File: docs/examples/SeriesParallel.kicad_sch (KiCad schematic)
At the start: 3 parts

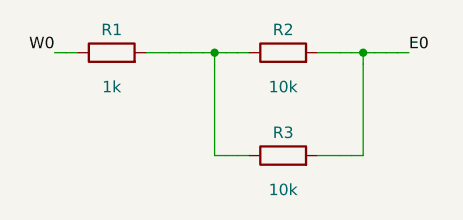
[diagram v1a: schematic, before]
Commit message: ERC-clean KiCad export: project + sym-lib-table, test points on open ports, automatic PWR_FLAGs from geometry nets; ERC (errors+warnings) asserted in tests
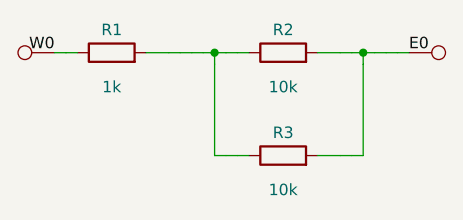
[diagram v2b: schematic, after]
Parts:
- added TP1, TP2: TestPoint, symbol Connector:TestPoint
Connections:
- net E0: now also TP1.1
- net W0: now also TP2.1
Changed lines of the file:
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@@
 		(instances
 			(project "SeriesParallel"
-				(path "/649ed304-67f7-4dcf-8923-cdace1b55596"
+				(path "/2fddaf15-e06a-4d6b-bdb8-eb01287d5898"
 					(reference "R1")
 					(unit 1)
@@
 		(instances
 			(project "SeriesParallel"
-				(path "/649ed304-67f7-4dcf-8923-cdace1b55596"
+				(path "/2fddaf15-e06a-4d6b-bdb8-eb01287d5898"
 					(reference "R2")
 					(unit 1)
@@
 		(instances
 			(project "SeriesParallel"
-				(path "/649ed304-67f7-4dcf-8923-cdace1b55596"
+				(path "/2fddaf15-e06a-4d6b-bdb8-eb01287d5898"
 					(reference "R3")
 					(unit 1)
 				)
+			)
+		)
+	)
+	(symbol
+		(lib_id "Connector:TestPoint")
+		(at 64.77 29.21 270)
+		(unit 1)
+		(exclude_from_sim yes)
+		(in_bom no)
+		(on_board yes)
+		(dnp no)
+		(property "Reference" "TP1"
+			(at 64.77 29.21 90)
+			(effects
+				(font
+					(size 1.27 1.27)
+				)
+				(hide yes)
+			)
+		)
+		(property "Value" "TestPoint"
+			(at 64.77 29.21 90)
+			(effects
+				(font
+					(size 1.27 1.27)
+				)
+				(hide yes)
+			)
+		)
+		(property "Footprint" ""
+			(at 64.77 29.21 90)
+			(effects
+				(font
+					(size 1.27 1.27)
+				)
+				(hide yes)
+			)
+		)
+		(property "Datasheet" ""
+			(at 64.77 29.21 90)
+			(effects
+				(font
+					(size 1.27 1.27)
+				)
+				(hide yes)
+			)
+		)
+		(pin "1"
+		)
+		(instances
+			(project "SeriesParallel"
+				(path "/2fddaf15-e06a-4d6b-bdb8-eb01287d5898"
+					(reference "TP1")
+					(unit 1)
+				)
+			)
+		)
+	)
+	(symbol
+		(lib_id "Connector:TestPoint")
+		(at 25.4 29.21 90)
+		(unit 1)
+		(exclude_from_sim yes)
+		(in_bom no)
+		(on_board yes)
+		(dnp no)
+		(property "Reference" "TP2"
+			(at 25.4 29.21 90)
+			(effects
+				(font
+					(size 1.27 1.27)
+				)
+				(hide yes)
+			)
+		)
+		(property "Value" "TestPoint"
+			(at 25.4 29.21 90)
+			(effects
+				(font
+					(size 1.27 1.27)
+				)
+				(hide yes)
+			)
+		)
+		(property "Footprint" ""
+			(at 25.4 29.21 90)
+			(effects
+				(font
+					(size 1.27 1.27)
+				)
+				(hide yes)
+			)
+		)
+		(property "Datasheet" ""
+			(at 25.4 29.21 90)
+			(effects
+				(font
+					(size 1.27 1.27)
+				)
+				(hide yes)
+			)
+		)
+		(pin "1"
+		)
+		(instances
+			(project "SeriesParallel"
+				(path "/2fddaf15-e06a-4d6b-bdb8-eb01287d5898"
+					(reference "TP2")
+					(unit 1)
+				)
